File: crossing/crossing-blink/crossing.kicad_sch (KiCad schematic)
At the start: 12 parts, among them Q2 2N3904, Q3 2N3904, SW1 SW_SPDT

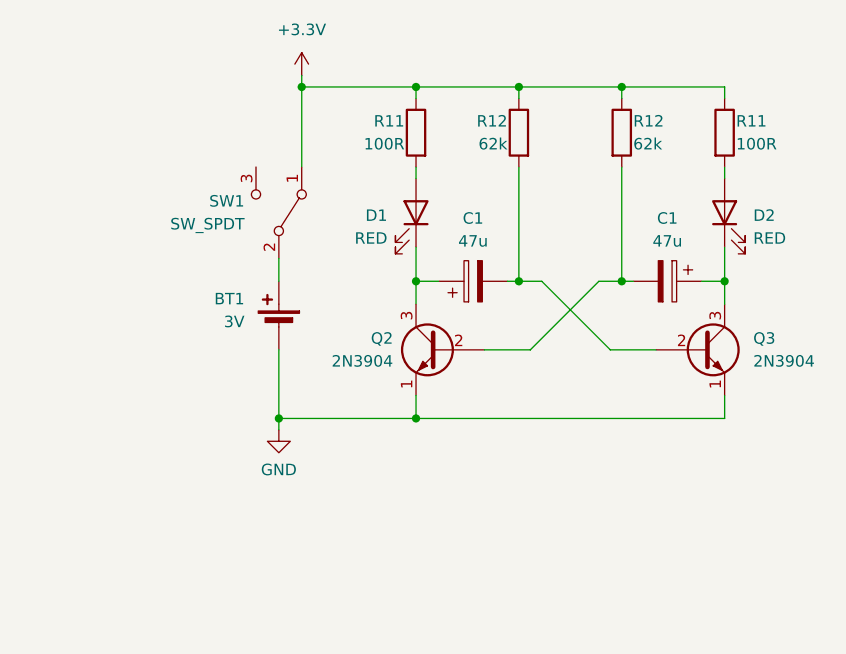
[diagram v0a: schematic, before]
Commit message: Finished crossing for production, modified other
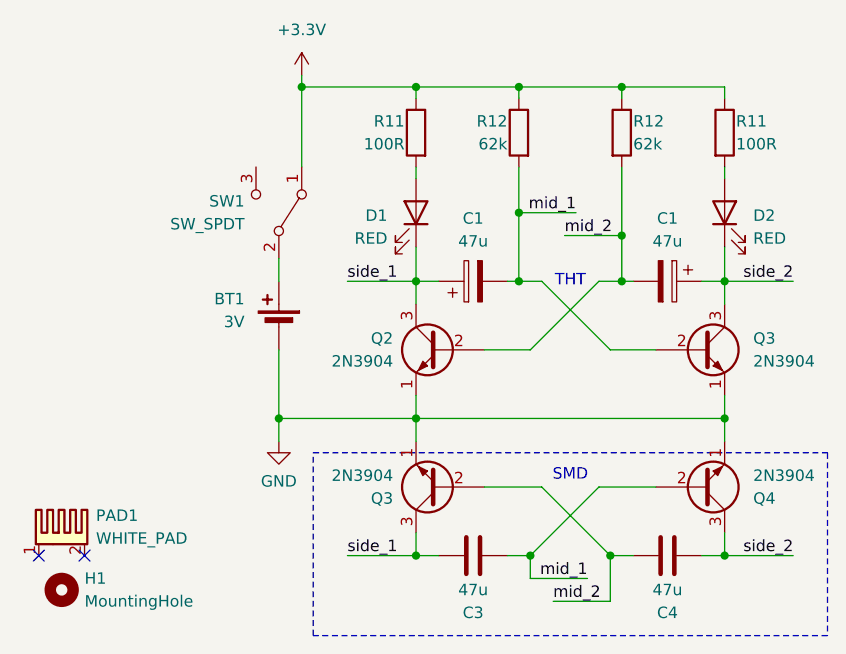
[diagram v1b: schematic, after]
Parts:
- added C3, C4: 47u, Capacitor_SMD:C_0805_2012Metric_Pad1.18x1.45mm_HandSolder, symbol Device:C
- added H1: MountingHole, MountingHole:MountingHole_2.2mm_M2_Pad, symbol Mechanical:MountingHole
- added PAD1: WHITE_PAD, lib:Touchpad_resistive, symbol Mechanical:Heatsink_Pad_2Pin
- added Q3, Q4: 2N3904, Package_TO_SOT_SMD:SOT-23, symbol Transistor_BJT:2N3904
- C1: footprint lib:CP_Radial_D6.3mm_P2.50mm+SMD_0805 -> Capacitor_THT:CP_Radial_D6.3mm_P2.50mm
- Q2, Q3: footprint lib:TO-92L_Inline_Wide+SMD_SOT-23 -> Package_TO_SOT_THT:TO-92L_Inline_Wide
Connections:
- net GND: now also Q3.1 (E), Q4.1 (E)
- net side_1: now reaches C1.1, D1.1 (K), Q2.3 (C)
- net side_1: now also C3.1, Q3.3 (C)
- net mid_2: now reaches C1.2, Q2.2 (B), R12.2
- net mid_2: now also C4.1, Q3.2 (B)
- net side_2: now reaches C1.1, D2.1 (K), Q3.3 (C)
- net side_2: now also C4.2, Q4.3 (C)
- net mid_1: now reaches C1.2, Q3.2 (B), R12.2
- net mid_1: now also C3.2, Q4.2 (B)
- no-connect marks 0 -> 2
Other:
- note added: "SMD"
- note added: "THT"

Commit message: Some interesting supermegachanges
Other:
- note added: "C1"
- note added: "C2"
- note added: "Q1"
- note added: "Q2"
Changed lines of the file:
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@@
+		)
+	)
+	(polyline
+		(pts
+			(xy 132.08 123.19) (xy 134.62 123.19)
+		)
+		(stroke
+			(width 0)
+			(type default)
 		)
 	)
@@
 		)
 	)
+	(polyline
+		(pts
+			(xy 142.24 135.89) (xy 144.78 135.89)
+		)
+		(stroke
+			(width 0)
+			(type default)
+		)
+	)
 	(wire
 		(pts
@@
 		)
 	)
+	(polyline
+		(pts
+			(xy 177.292 123.19) (xy 174.752 123.19)
+		)
+		(stroke
+			(width 0)
+			(type default)
+		)
+	)
 	(wire
 		(pts
@@
 		(pts
 			(xy 124.46 77.47) (xy 137.16 77.47)
+		)
+		(stroke
+			(width 0)
+			(type default)
+		)
+	)
+	(polyline
+		(pts
+			(xy 163.83 135.89) (xy 166.37 135.89)
 		)
 		(stroke
@@
 		(effects
 			(font
+				(size 1.27 1.27)
+			)
+		)
+	)
+	(text "C1"
+		(exclude_from_sim no)
+		(at 140.462 136.144 0)
+		(effects
+			(font
+				(size 1.27 1.27)
+			)
+		)
+	)
+	(text "Q2\n"
+		(exclude_from_sim no)
+		(at 179.07 123.444 0)
+		(effects
+			(font
+				(size 1.27 1.27)
+			)
+		)
+	)
+	(text "Q1"
+		(exclude_from_sim no)
+		(at 130.302 123.444 0)
+		(effects
+			(font
+				(size 1.27 1.27)
+			)
+		)
+	)
+	(text "C2"
+		(exclude_from_sim no)
+		(at 162.052 136.144 0)
+		(effects
+			(font

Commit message: Some updates, added new library symbols/fps.
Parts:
- renumbered C1 to C2, Q2 to Q1, Q3 to Q2, R11 to R1, R12 to R2, R12 to R3, R11 to R4
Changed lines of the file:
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@@
 (kicad_sch
-	(version 20231120)
+	(version 20250114)
 	(generator "eeschema")
-	(generator_version "8.0")
+	(generator_version "9.0")
 	(paper "A4")
+	(rectangle
+		(start 125.73 118.11)
+		(end 182.88 138.43)
+		(stroke
+			(width 0)
+			(type dash)
+		)
+		(fill
+			(type none)
+		)
+	)
+	(text "THT"
+		(exclude_from_sim no)
+		(at 154.305 99.06 0)
+		(effects
+			(font
+				(size 1.27 1.27)
+			)
+		)
+	)
+	(text "C1"
+		(exclude_from_sim no)
+		(at 140.462 136.144 0)
+		(effects
+			(font
+				(size 1.27 1.27)
+			)
+		)
+	)
+	(text "Q2\n"
+		(exclude_from_sim no)
+		(at 179.07 123.444 0)
+		(effects
+			(font
+				(size 1.27 1.27)
+			)
+		)
+	)
+	(text "Q1"
+		(exclude_from_sim no)
+		(at 130.302 123.444 0)
+		(effects
+			(font
+				(size 1.27 1.27)
+			)
+		)
+	)
+	(text "C2"
+		(exclude_from_sim no)
+		(at 162.052 136.144 0)
+		(effects
+			(font
+				(size 1.27 1.27)
+			)
+		)
+	)
+	(text "SMD"
+		(exclude_from_sim no)
+		(at 154.305 120.65 0)
+		(effects
+			(font
+				(size 1.27 1.27)
+			)
+		)
+	)
 	(junction
 		(at 137.16 129.54)
@@
 		)
 	)
-	(rectangle
-		(start 125.73 118.11)
-		(end 182.88 138.43)
-		(stroke
-			(width 0)
-			(type dash)
-		)
-		(fill
-			(type none)
-		)
-	)
-	(text "THT"
-		(exclude_from_sim no)
-		(at 154.305 99.06 0)
+	(label "side_2"
+		(at 179.07 99.06 180)
 		(effects
 			(font
 				(size 1.27 1.27)
 			)
-		)
-	)
-	(text "C1"
-		(exclude_from_sim no)
-		(at 140.462 136.144 0)
+			(justify right bottom)
+		)
+	)
+	(label "mid_2"
+		(at 153.67 93.98 0)
 		(effects
 			(font
 				(size 1.27 1.27)
 			)
-		)
-	)
-	(text "Q2\n"
-		(exclude_from_sim no)
-		(at 179.07 123.444 0)
+			(justify left bottom)
+		)
+	)
+	(label "side_1"
+		(at 129.54 99.06 0)
 		(effects
 			(font
 				(size 1.27 1.27)
 			)
-		)
-	)
-	(text "Q1"
-		(exclude_from_sim no)
-		(at 130.302 123.444 0)
+			(justify left bottom)
+		)
+	)
+	(label "mid_2"
+		(at 152.4 134.62 0)
 		(effects
 			(font
 				(size 1.27 1.27)
 			)
-		)
-	)
-	(text "C2"
-		(exclude_from_sim no)
-		(at 162.052 136.144 0)
+			(justify left bottom)
+		)
+	)
+	(label "mid_1"
+		(at 154.94 91.44 180)
 		(effects
 			(font
 				(size 1.27 1.27)
 			)
-		)
-	)
-	(text "SMD"
-		(exclude_from_sim no)
-		(at 154.305 120.65 0)
+			(justify right bottom)
+		)
+	)
+	(label "mid_1"
+		(at 156.21 132.08 180)
 		(effects
 			(font
 				(size 1.27 1.27)
 			)
-		)
-	)
-	(label "side_2"
-		(at 179.07 99.06 180)
-		(fields_autoplaced yes)
+			(justify right bottom)
+		)
+	)
+	(label "side_1"
+		(at 129.54 129.54 0)
 		(effects
 			(font
 				(size 1.27 1.27)
 			)
-			(justify right bottom)
-		)
-	)
-	(label "mid_2"
-		(at 153.67 93.98 0)
-		(fields_autoplaced yes)
-		(effects
-			(font
-				(size 1.27 1.27)
-			)
-			(justify left bottom)
-		)
-	)
-	(label "side_1"
-		(at 129.54 99.06 0)
-		(fields_autoplaced yes)
-		(effects
-			(font
-				(size 1.27 1.27)
-			)
-			(justify left bottom)
-		)
-	)
-	(label "mid_2"
-		(at 152.4 134.62 0)
-		(fields_autoplaced yes)
-		(effects
-			(font
-				(size 1.27 1.27)
-			)
-			(justify left bottom)
-		)
-	)
-	(label "mid_1"
-		(at 154.94 91.44 180)
-		(fields_autoplaced yes)
-		(effects
-			(font
-				(size 1.27 1.27)
-			)
-			(justify right bottom)
-		)
-	)
-	(label "mid_1"
-		(at 156.21 132.08 180)
-		(fields_autoplaced yes)
-		(effects
-			(font
-				(size 1.27 1.27)
-			)
-			(justify right bottom)
-		)
-	)
-	(label "side_1"
-		(at 129.54 129.54 0)
-		(fields_autoplaced yes)
-		(effects
-			(font
-				(size 1.27 1.27)
-			)
 			(justify left bottom)
 		)
@@
 	(label "side_2"
 		(at 179.07 129.54 180)
-		(fields_autoplaced yes)
 		(effects
 			(font
@@
 		(on_board yes)
 		(dnp no)
-		(property "Reference" "R12"
+		(property "Reference" "R3"
 			(at 161.29 81.28 0)
 			(effects
@@
 		(dnp no)
 		(fields_autoplaced yes)
-		(property "Reference" "#PWR012"
+		(property "Reference" "#PWR02"
 			(at 121.92 123.19 0)
 			(effects
@@
 		(on_board yes)
 		(dnp no)
-		(property "Reference" "R11"
+		(property "Reference" "R1"
 			(at 135.89 81.28 0)
 			(effects
@@
 		(on_board yes)
 		(dnp no)
-		(property "Reference" "Q2"
+		(property "Reference" "Q1"
 			(at 134.62 105.41 0)
 			(effects
@@
 		(on_board yes)
 		(dnp no)
-		(property "Reference" "R12"
+		(property "Reference" "R2"
 			(at 147.32 81.28 0)
 			(effects
@@
 		(dnp no)
 		(fields_autoplaced yes)
-		(property "Reference" "Q3"
+		(property "Reference" "Q2"
 			(at 174.625 105.41 0)
 			(effects
@@
 		(on_board yes)
 		(dnp no)
-		(property "Reference" "R11"
+		(property "Reference" "R4"
 			(at 172.72 81.28 0)
 			(effects
@@
 		(on_board yes)
 		(dnp no)
-		(property "Reference" "C1"
+		(property "Reference" "C2"
 			(at 165.1 92.075 90)
 			(effects
@@
 		)
 	)
+	(embedded_fonts no)
 )
